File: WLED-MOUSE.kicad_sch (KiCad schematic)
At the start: 21 parts, among them J1 FTDI-header, J2 Power-in, J4 Pixel-strip, J6 Pixel-strip, J7 Pixel-strip, J8 Pixel-strip, M1 INMP441, M2 INMP441-TH, Q1 NDT3055L, SW1 SW_MEC_5E, SW2 SW_MEC_5E, U1 ESP32-WROOM-32D, U2 ESP32-WROOM-32D, U3 SN74LV4T125

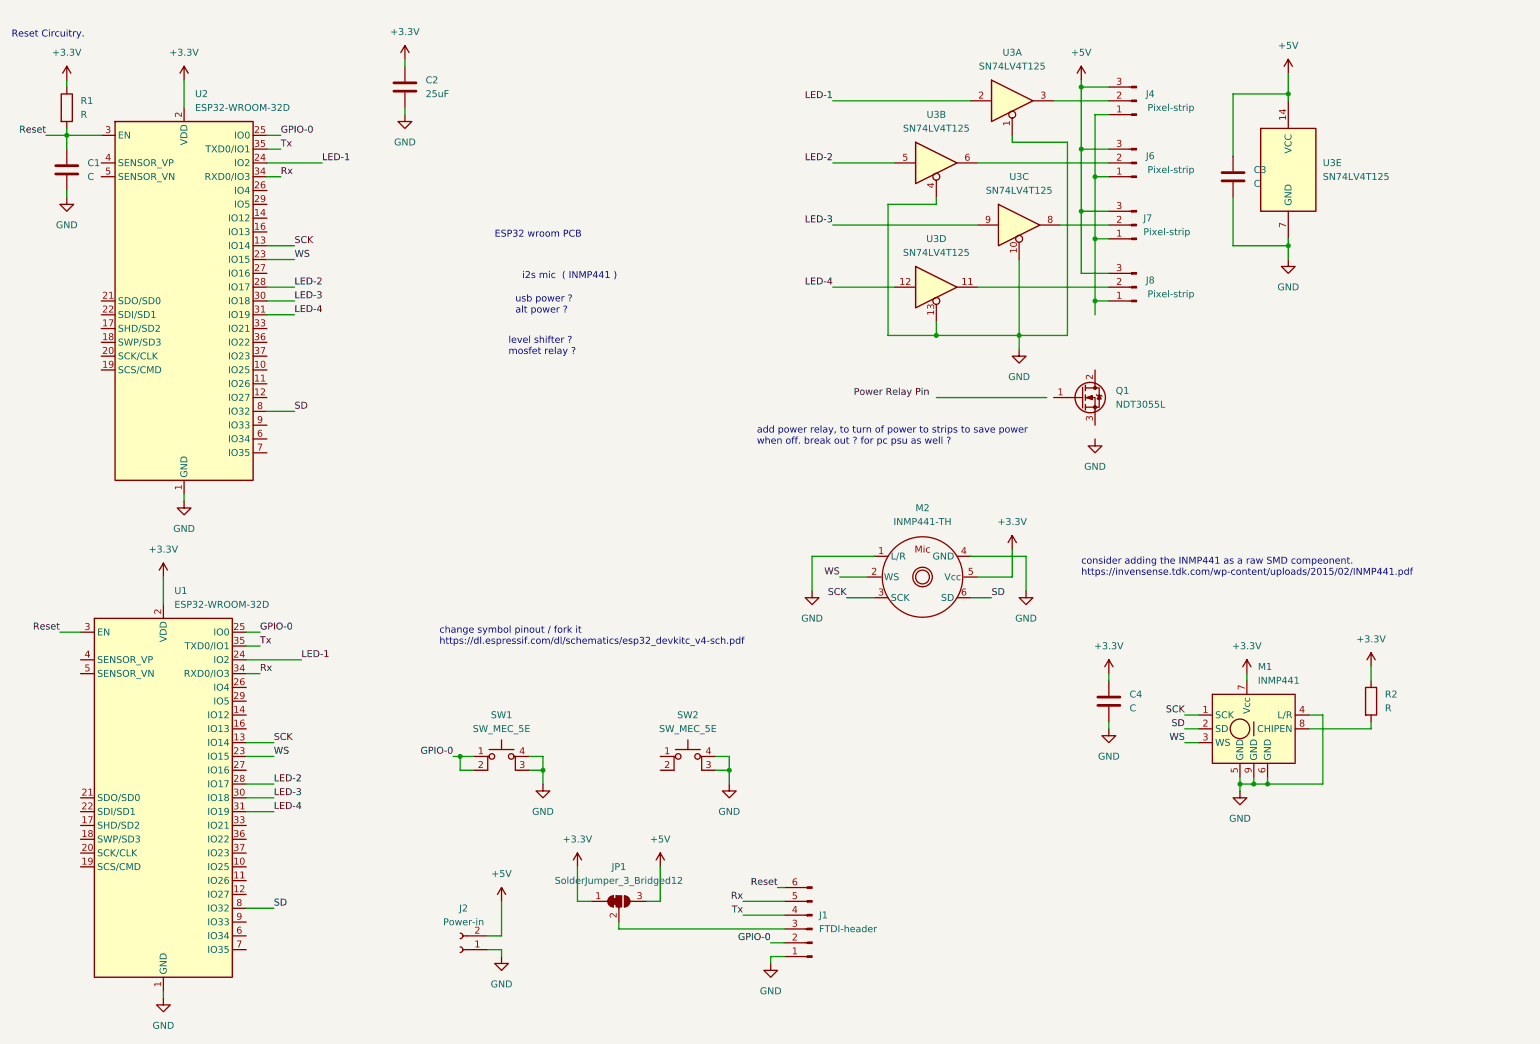
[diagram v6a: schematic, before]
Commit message: added GPIO names, to silk screen, to make life easier when using the board.
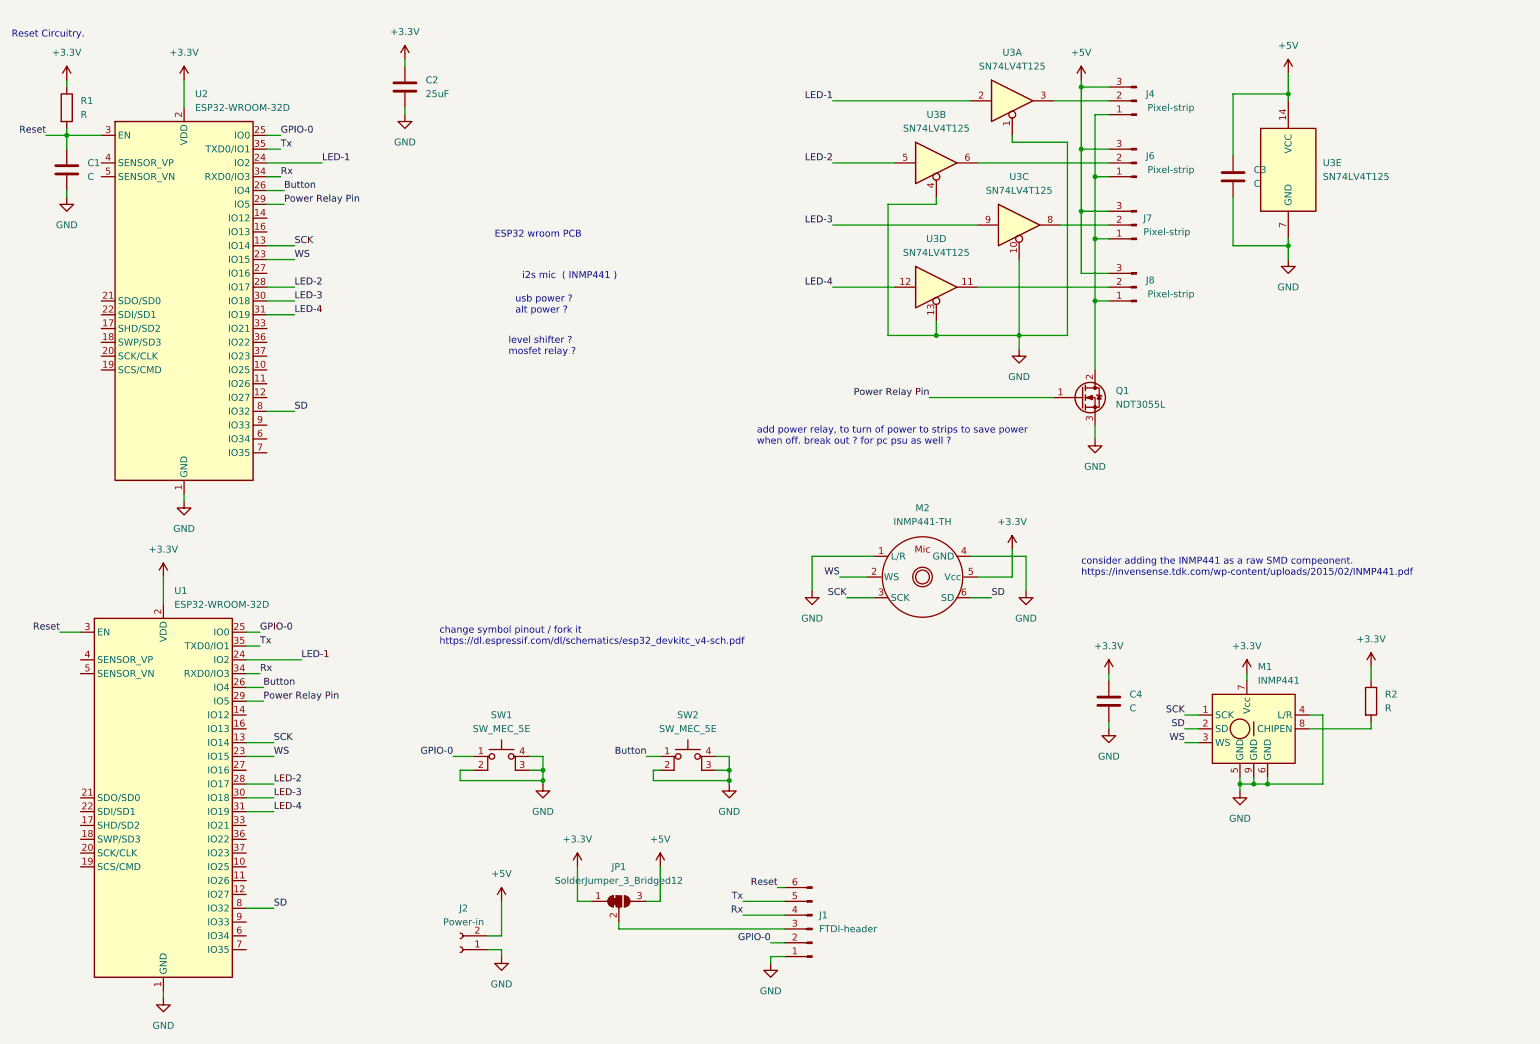
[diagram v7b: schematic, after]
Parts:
- SW1, SW2: footprint Button_Switch_THT:SW_PUSH_6mm_H5mm -> Button_Switch_THT:SW_PUSH_6mm
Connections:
- net GND: now also Q1.3 (S), SW1.2, SW2.2
- net GPIO-0: no longer SW1.2
- net Power Relay Pin: now also Q1.1 (G), U1.29 (IO5), U2.29 (IO5)
- net Rx: now also J1.4 (Pin_4); no longer J1.5 (Pin_5)
- net Tx: now also J1.5 (Pin_5); no longer J1.4 (Pin_4)
- net at Q1.2 (D): now also J4.1 (Pin_1), J6.1 (Pin_1), J7.1 (Pin_1), J8.1 (Pin_1)
- net Button: now reaches U1.26 (IO4)
- net Button: now also SW2.1, U2.26 (IO4)
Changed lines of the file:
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@@
 (kicad_sch (version 20211123) (generator eeschema)
   (paper "A4")
-  (junction (at 101.6 149.86) (diameter 0) (color 0 0 0 0)
-  )
   (junction (at 29.21 35.56) (diameter 0) (color 0 0 0 0)
   )
@@
   (junction (at 250.19 154.94) (diameter 0) (color 0 0 0 0)
   )
+  (junction (at 116.84 154.305) (diameter 0) (color 0 0 0 0)
+  )
   (junction (at 215.9 38.1) (diameter 0) (color 0 0 0 0)
   )
+  (junction (at 151.13 154.305) (diameter 0) (color 0 0 0 0)
+  )
   (junction (at 189.23 72.39) (diameter 0) (color 0 0 0 0)
   )
@@
     (stroke (width 0) (type default) (color 0 0 0 0))
   )
+  (wire (pts (xy 135.89 149.86) (xy 138.43 149.86))
+    (stroke (width 0) (type default) (color 0 0 0 0))
+  )
   (wire (pts (xy 66.04 40.64) (xy 76.2 40.64))
     (stroke (width 0) (type default) (color 0 0 0 0))
@@
     (stroke (width 0) (type default) (color 0 0 0 0))
   )
+  (wire (pts (xy 66.04 45.72) (xy 69.215 45.72))
+    (stroke (width 0) (type default) (color 0 0 0 0))
+  )
   (wire (pts (xy 218.44 31.75) (xy 218.44 43.18))
     (stroke (width 0) (type default) (color 0 0 0 0))
@@
     (stroke (width 0) (type default) (color 0 0 0 0))
   )
-  (wire (pts (xy 101.6 149.86) (xy 104.14 149.86))
+  (wire (pts (xy 100.33 149.86) (xy 104.14 149.86))
     (stroke (width 0) (type default) (color 0 0 0 0))
   )
@@
     (stroke (width 0) (type default) (color 0 0 0 0))
   )
-  (wire (pts (xy 101.6 149.86) (xy 101.6 152.4))
-    (stroke (width 0) (type default) (color 0 0 0 0))
-  )
   (wire (pts (xy 170.18 52.07) (xy 196.85 52.07))
     (stroke (width 0) (type default) (color 0 0 0 0))
@@
     (stroke (width 0) (type default) (color 0 0 0 0))
   )
+  (wire (pts (xy 138.43 152.4) (xy 137.16 152.4))
+    (stroke (width 0) (type default) (color 0 0 0 0))
+  )
   (wire (pts (xy 254 27.94) (xy 254 29.21))
     (stroke (width 0) (type default) (color 0 0 0 0))
@@
     (stroke (width 0) (type default) (color 0 0 0 0))
   )
+  (wire (pts (xy 66.04 48.26) (xy 69.215 48.26))
+    (stroke (width 0) (type default) (color 0 0 0 0))
+  )
   (wire (pts (xy 138.43 176.53) (xy 138.43 170.18))
     (stroke (width 0) (type default) (color 0 0 0 0))
@@
     (stroke (width 0) (type default) (color 0 0 0 0))
   )
+  (wire (pts (xy 151.13 154.305) (xy 151.13 154.94))
+    (stroke (width 0) (type default) (color 0 0 0 0))
+  )
+  (wire (pts (xy 218.44 88.9) (xy 218.44 91.44))
+    (stroke (width 0) (type default) (color 0 0 0 0))
+  )
   (wire (pts (xy 29.21 25.4) (xy 29.21 26.67))
     (stroke (width 0) (type default) (color 0 0 0 0))
@@
     (stroke (width 0) (type default) (color 0 0 0 0))
   )
+  (wire (pts (xy 62.23 137.16) (xy 65.405 137.16))
+    (stroke (width 0) (type default) (color 0 0 0 0))
+  )
   (wire (pts (xy 166.37 113.03) (xy 166.37 119.38))
     (stroke (width 0) (type default) (color 0 0 0 0))
@@
     (stroke (width 0) (type default) (color 0 0 0 0))
   )
-  (wire (pts (xy 116.84 152.4) (xy 116.84 154.94))
-    (stroke (width 0) (type default) (color 0 0 0 0))
-  )
-  (wire (pts (xy 189.23 83.82) (xy 209.55 83.82))
+  (wire (pts (xy 116.84 152.4) (xy 116.84 154.305))
+    (stroke (width 0) (type default) (color 0 0 0 0))
+  )
+  (wire (pts (xy 187.96 83.82) (xy 210.82 83.82))
     (stroke (width 0) (type default) (color 0 0 0 0))
   )
@@
     (stroke (width 0) (type default) (color 0 0 0 0))
   )
+  (wire (pts (xy 101.6 154.305) (xy 116.84 154.305))
+    (stroke (width 0) (type default) (color 0 0 0 0))
+  )
   (wire (pts (xy 161.29 181.61) (xy 130.81 181.61))
     (stroke (width 0) (type default) (color 0 0 0 0))
   )
-  (wire (pts (xy 218.44 66.04) (xy 218.44 68.58))
+  (wire (pts (xy 218.44 66.04) (xy 218.44 78.74))
     (stroke (width 0) (type default) (color 0 0 0 0))
   )
@@
     (stroke (width 0) (type default) (color 0 0 0 0))
   )
+  (wire (pts (xy 101.6 152.4) (xy 101.6 154.305))
+    (stroke (width 0) (type default) (color 0 0 0 0))
+  )
   (wire (pts (xy 260.35 154.94) (xy 250.19 154.94))
     (stroke (width 0) (type default) (color 0 0 0 0))
@@
     (stroke (width 0) (type default) (color 0 0 0 0))
   )
+  (wire (pts (xy 62.23 139.7) (xy 65.405 139.7))
+    (stroke (width 0) (type default) (color 0 0 0 0))
+  )
   (wire (pts (xy 62.23 129.54) (xy 64.77 129.54))
     (stroke (width 0) (type default) (color 0 0 0 0))
@@
     (stroke (width 0) (type default) (color 0 0 0 0))
   )
-  (wire (pts (xy 100.33 149.86) (xy 101.6 149.86))
-    (stroke (width 0) (type default) (color 0 0 0 0))
-  )
   (wire (pts (xy 234.95 144.78) (xy 237.49 144.78))
     (stroke (width 0) (type default) (color 0 0 0 0))
@@
     (stroke (width 0) (type default) (color 0 0 0 0))
   )
-  (wire (pts (xy 151.13 152.4) (xy 151.13 154.94))
+  (wire (pts (xy 151.13 152.4) (xy 151.13 154.305))
     (stroke (width 0) (type default) (color 0 0 0 0))
   )
@@
     (stroke (width 0) (type default) (color 0 0 0 0))
   )
+  (wire (pts (xy 137.16 152.4) (xy 137.16 154.305))
+    (stroke (width 0) (type default) (color 0 0 0 0))
+  )
   (wire (pts (xy 204.47 58.42) (xy 204.47 72.39))
     (stroke (width 0) (type default) (color 0 0 0 0))
@@
     (stroke (width 0) (type default) (color 0 0 0 0))
   )
+  (wire (pts (xy 116.84 154.305) (xy 116.84 154.94))
+    (stroke (width 0) (type default) (color 0 0 0 0))
+  )
   (wire (pts (xy 62.23 134.62) (xy 64.77 134.62))
     (stroke (width 0) (type default) (color 0 0 0 0))
@@
   )
   (wire (pts (xy 243.84 46.99) (xy 243.84 55.88))
+    (stroke (width 0) (type default) (color 0 0 0 0))
+  )
+  (wire (pts (xy 137.16 154.305) (xy 151.13 154.305))
     (stroke (width 0) (type default) (color 0 0 0 0))
   )
@@
     (effects (font (size 1.27 1.27)) (justify left bottom))
   )
+  (label "Button" (at 65.405 137.16 0)
+    (effects (font (size 1.27 1.27)) (justify left bottom))
+  )
   (label "SD" (at 67.31 177.8 0)
     (effects (font (size 1.27 1.27)) (justify left bottom))
@@
     (effects (font (size 1.27 1.27)) (justify left bottom))
   )
+  (label "Button" (at 135.89 149.86 180)
+    (effects (font (size 1.27 1.27)) (justify right bottom))
+  )
   (label "SCK" (at 172.72 120.65 180)
     (effects (font (size 1.27 1.27)) (justify right bottom))
   )
-  (label "Tx" (at 153.67 179.07 180)
+  (label "Tx" (at 153.67 176.53 180)
     (effects (font (size 1.27 1.27)) (justify right bottom))
   )
@@
     (effects (font (size 1.27 1.27)) (justify left bottom))
   )
+  (label "Power Relay Pin" (at 65.405 139.7 0)
+    (effects (font (size 1.27 1.27)) (justify left bottom))
+  )
   (label "LED-1" (at 170.18 29.21 180)
     (effects (font (size 1.27 1.27)) (justify right bottom))
@@
     (effects (font (size 1.27 1.27)) (justify right bottom))
   )
-  (label "Rx" (at 153.67 176.53 180)
+  (label "Rx" (at 153.67 179.07 180)
     (effects (font (size 1.27 1.27)) (justify right bottom))
   )
@@
     (effects (font (size 1.27 1.27)) (justify right bottom))
   )
+  (label "Button" (at 69.215 45.72 0)
+    (effects (font (size 1.27 1.27)) (justify left bottom))
+  )
   (label "LED-3" (at 67.31 157.48 0)
     (effects (font (size 1.27 1.27)) (justify left bottom))
@@
   (label "GPIO-0" (at 100.33 149.86 180)
     (effects (font (size 1.27 1.27)) (justify right bottom))
+  )
+  (label "Power Relay Pin" (at 69.215 48.26 0)
+    (effects (font (size 1.27 1.27)) (justify left bottom))
   )
   (label "Tx" (at 64.77 129.54 0)
@@
     (pin "6")
   )
+  (symbol (lib_id "Switch:SW_MEC_5E") (at 143.51 152.4 0) (unit 1)
+    (in_bom yes) (on_board yes) (fields_autoplaced)
+    (property "Reference" "SW2" (id 0) (at 143.51 142.24 0))
+    (property "Value" "SW_MEC_5E" (id 1) (at 143.51 144.78 0))
+    (property "Footprint" "Button_Switch_THT:SW_PUSH_6mm" (id 2) (at 143.51 144.78 0)
+      (effects (font (size 1.27 1.27)) hide)
+    )
+    (property "Datasheet" "http://www.apem.com/int/index.php?controller=attachment&id_attachment=1371" (id 3) (at 143.51 144.78 0)
+      (effects (font (size 1.27 1.27)) hide)
+    )
+    (pin "1")
+    (pin "2")
+    (pin "3")
+    (pin "4")
+  )
   (symbol (lib_id "power:+3.3V") (at 246.38 134.62 0) (unit 1)
     (in_bom yes) (on_board yes) (fields_autoplaced)
@@
     (property "Reference" "SW1" (id 0) (at 109.22 142.24 0))
     (property "Value" "SW_MEC_5E" (id 1) (at 109.22 144.78 0))
-    (property "Footprint" "Button_Switch_THT:SW_PUSH_6mm_H5mm" (id 2) (at 109.22 144.78 0)
+    (property "Footprint" "Button_Switch_THT:SW_PUSH_6mm" (id 2) (at 109.22 144.78 0)
       (effects (font (size 1.27 1.27)) hide)
     )
@@
     (pin "1")
   )
-  (symbol (lib_id "Switch:SW_MEC_5E") (at 143.51 152.4 0) (unit 1)
-    (in_bom yes) (on_board yes) (fields_autoplaced)
-    (property "Reference" "SW2" (id 0) (at 143.51 142.24 0))
-    (property "Value" "SW_MEC_5E" (id 1) (at 143.51 144.78 0))
-    (property "Footprint" "Button_Switch_THT:SW_PUSH_6mm_H5mm" (id 2) (at 143.51 144.78 0)
-      (effects (font (size 1.27 1.27)) hide)
-    )
-    (property "Datasheet" "http://www.apem.com/int/index.php?controller=attachment&id_attachment=1371" (id 3) (at 143.51 144.78 0)
-      (effects (font (size 1.27 1.27)) hide)
-    )
-    (pin "1")
-    (pin "2")
-    (pin "3")
-    (pin "4")
-  )
   (symbol (lib_id "power:GND") (at 50.8 102.87 0) (unit 1)
     (in_bom yes) (on_board yes) (fields_autoplaced)
@@
     )
     (path "/c9259e24-c18c-495f-a2f3-35feb5c40597"
-      (reference "SW1") (unit 1) (value "SW_MEC_5E") (footprint "Button_Switch_THT:SW_PUSH_6mm_H5mm")
-    )
-    (path "/f1032ec7-7136-4381-b378-9a74c0aa0e18"
-      (reference "SW2") (unit 1) (value "SW_MEC_5E") (footprint "Button_Switch_THT:SW_PUSH_6mm_H5mm")
+      (reference "SW1") (unit 1) (value "SW_MEC_5E") (footprint "Button_Switch_THT:SW_PUSH_6mm")
+    )
+    (path "/aa8eb5b2-1c06-4d61-80e6-b011d6fd5531"
+      (reference "SW2") (unit 1) (value "SW_MEC_5E") (footprint "Button_Switch_THT:SW_PUSH_6mm")
     )
     (path "/70f3e024-3cd8-4941-9e88-8fd7c03e5650"
